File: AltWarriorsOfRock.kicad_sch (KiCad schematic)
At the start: 19 parts, among them J1 Fret Board, J2 PM20205HBDN, J3 PM20203HBDN, J5 Debug, U1 ESP32-S3-WROOM-1

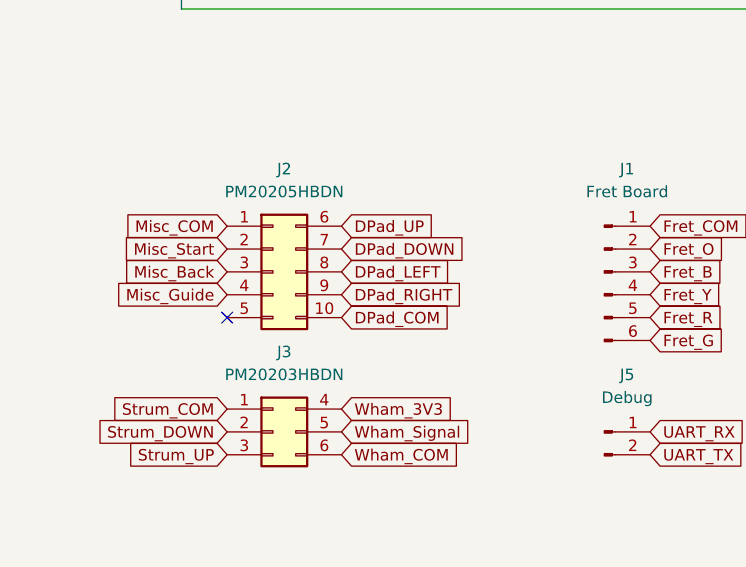
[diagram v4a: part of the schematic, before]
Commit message: Redo layout with all components topside
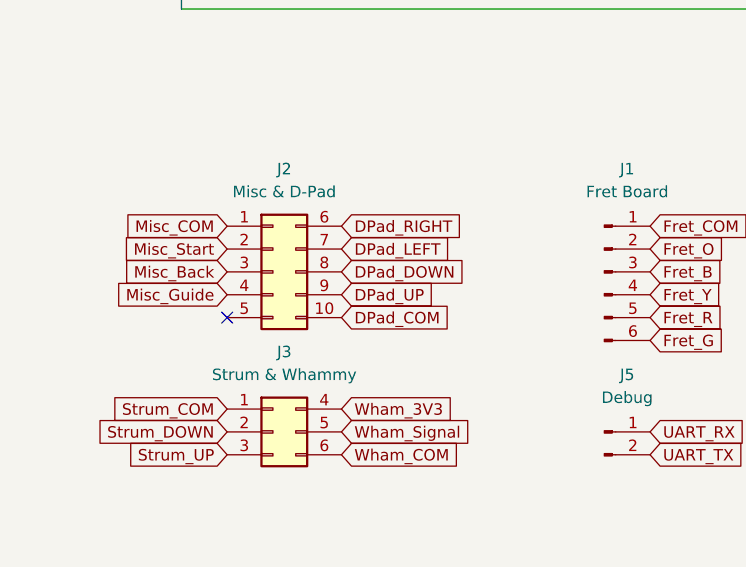
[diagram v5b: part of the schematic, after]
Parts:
- J2: value PM20205HBDN -> Misc & D-Pad; footprint Connector_Metz_ygaskh:PM20205HBDN -> Library_ygaskh:PinHeader_2x05_P2.54mm_Vertical_TopBottom
- J3: value PM20203HBDN -> Strum & Whammy; footprint Connector_Metz_ygaskh:PM20203HBDN -> Library_ygaskh:PinHeader_2x03_P2.54mm_Vertical_TopBottom
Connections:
- net DPad_DOWN: now also J2.8 (Pin_8); no longer J2.7 (Pin_7)
- net DPad_LEFT: now also J2.7 (Pin_7); no longer J2.8 (Pin_8)
- net DPad_RIGHT: now also J2.6 (Pin_6); no longer J2.9 (Pin_9)
- net DPad_UP: now also J2.9 (Pin_9); no longer J2.6 (Pin_6)

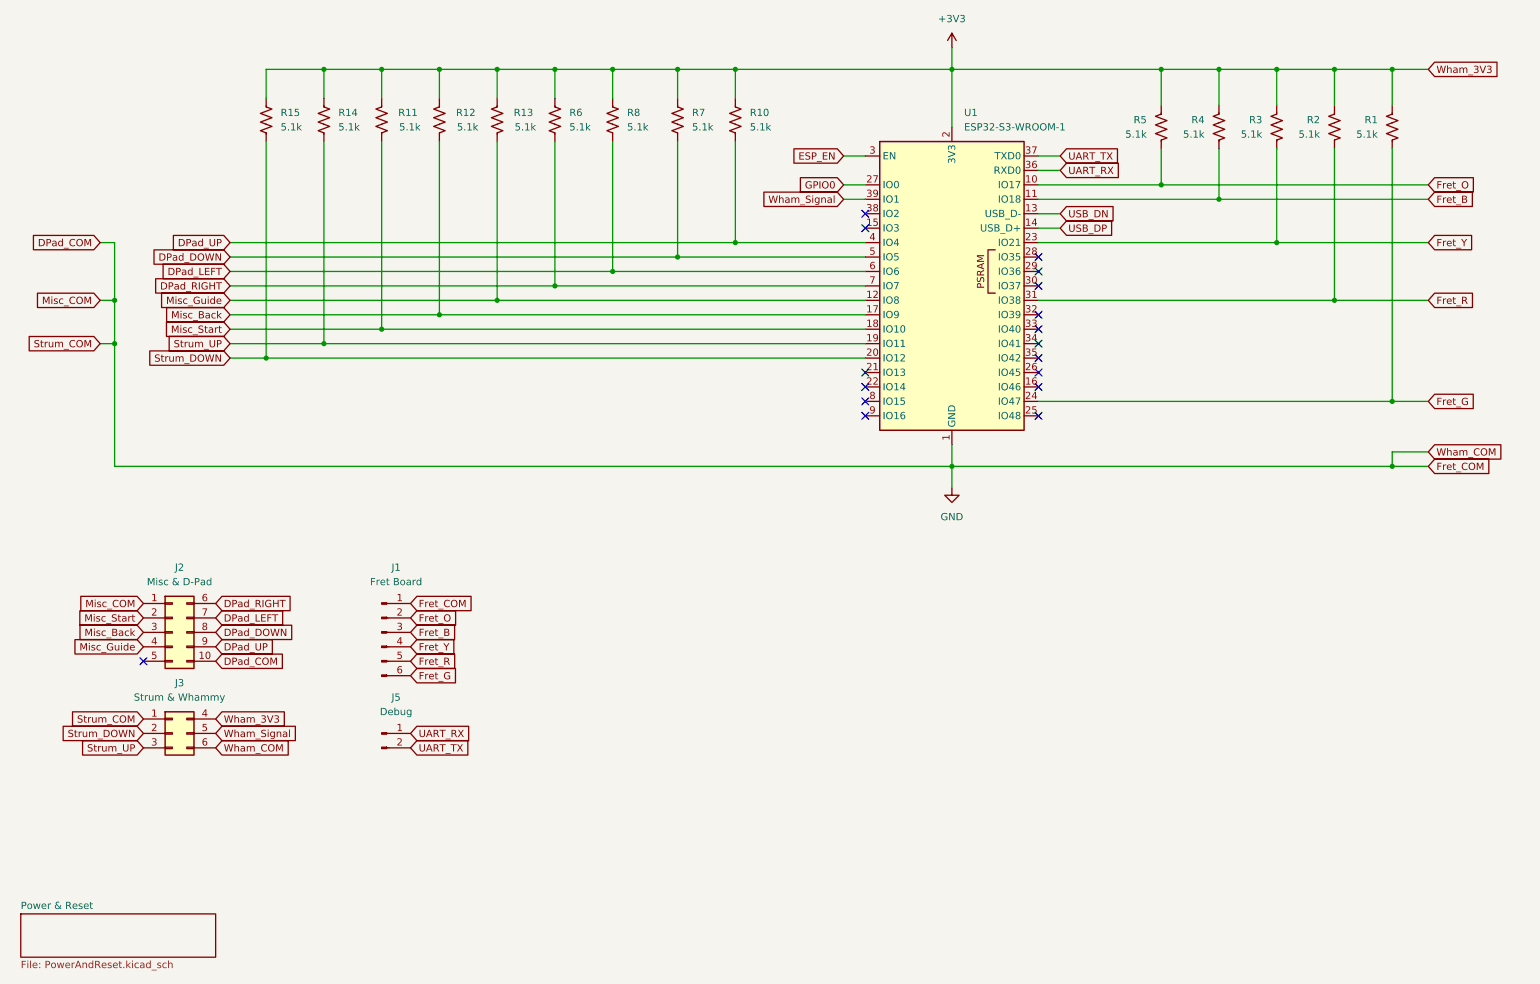
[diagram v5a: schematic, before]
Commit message: Adjust schematic 'no connect' symbols to prevent overlap
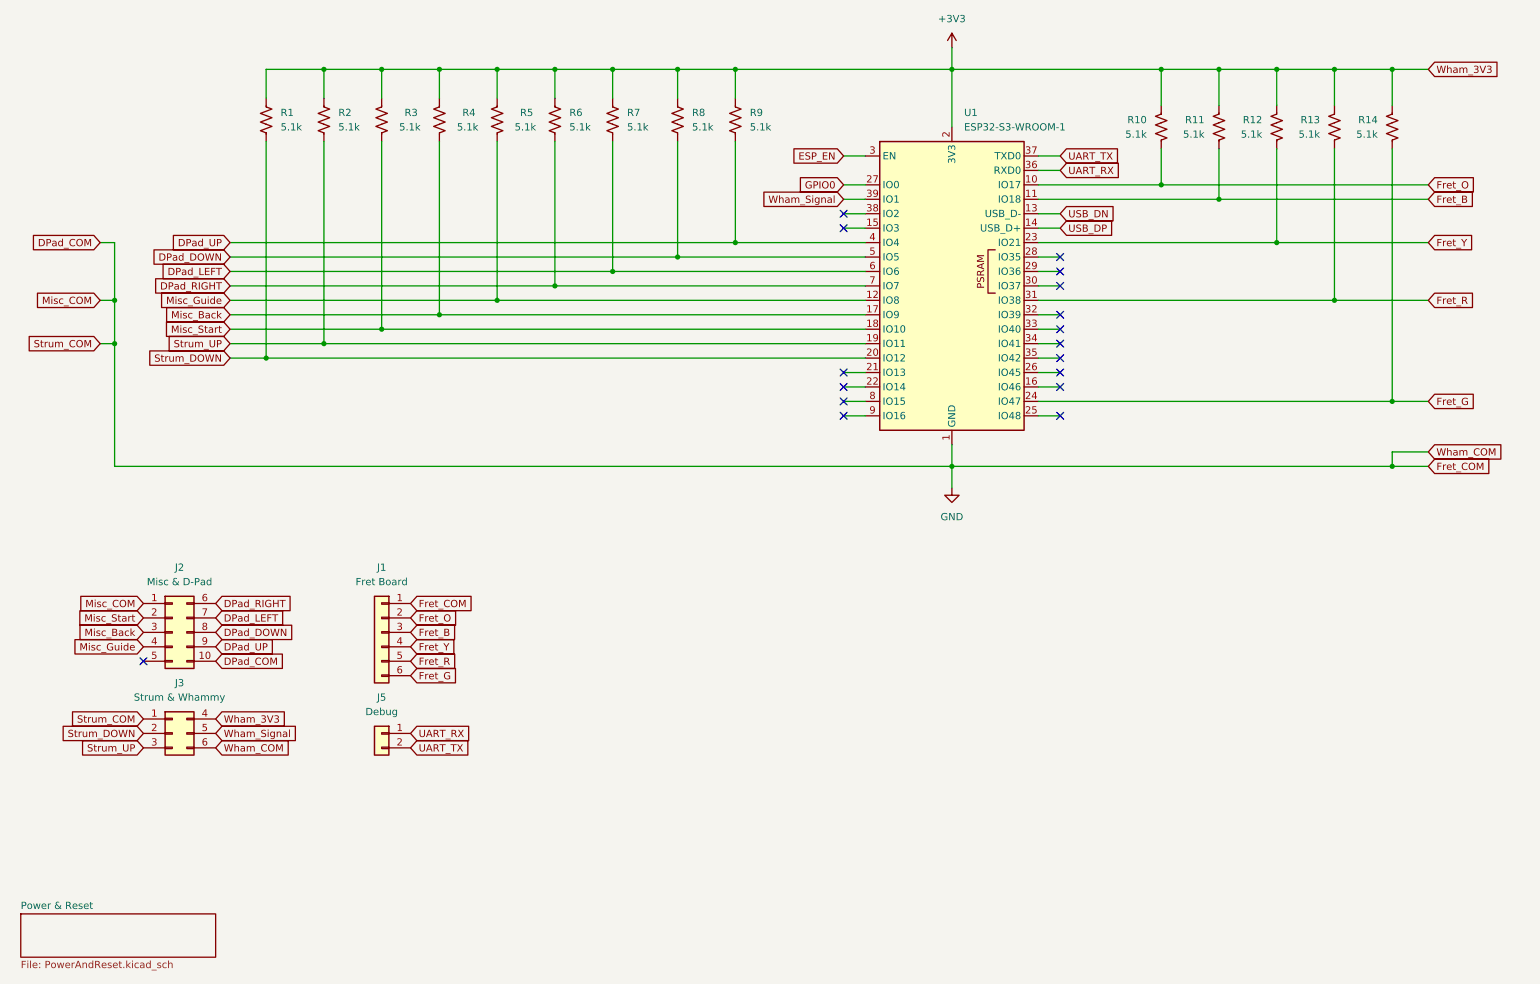
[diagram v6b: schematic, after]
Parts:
- J1: symbol Connector:Conn_01x06_Pin -> Connector_Generic:Conn_01x06
- J5: symbol Connector:Conn_01x02_Pin -> Connector_Generic:Conn_01x02
- renumbered R15 to R1, R5 to R10, R4 to R11, R3 to R12, R2 to R13, R1 to R14, R14 to R2, R11 to R3, R12 to R4, R13 to R5, R8 to R7, R7 to R8, R10 to R9
